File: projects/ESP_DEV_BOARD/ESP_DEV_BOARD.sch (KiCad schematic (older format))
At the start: 34 parts, among them CN1 MJ-179P, CN2 B6B-XH-A, CN3 DM3AT-SF-PEJM5, CN7 PH-1X10RG(2), SW1 SKHHBY, SW2 SKHHBY, SW3 SKHHBY, SW4 SKHHBY, U1 BME680, U2 CCS811

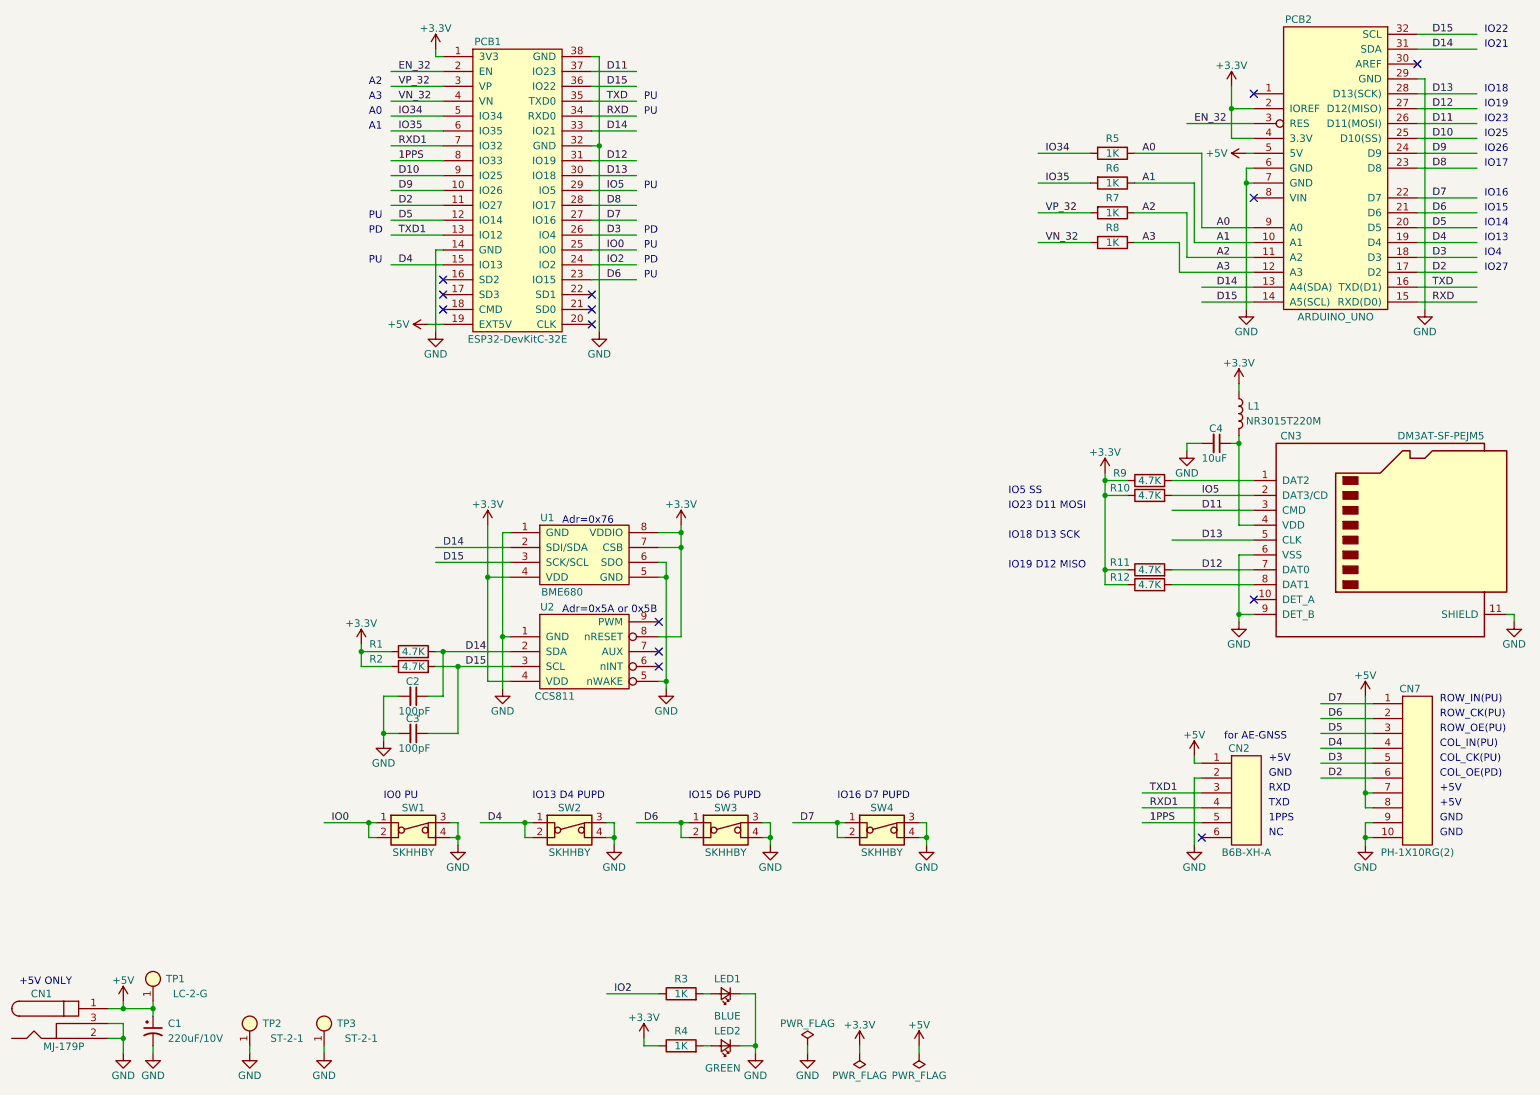
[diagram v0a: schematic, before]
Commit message: 赤外線送受信回路の追加。
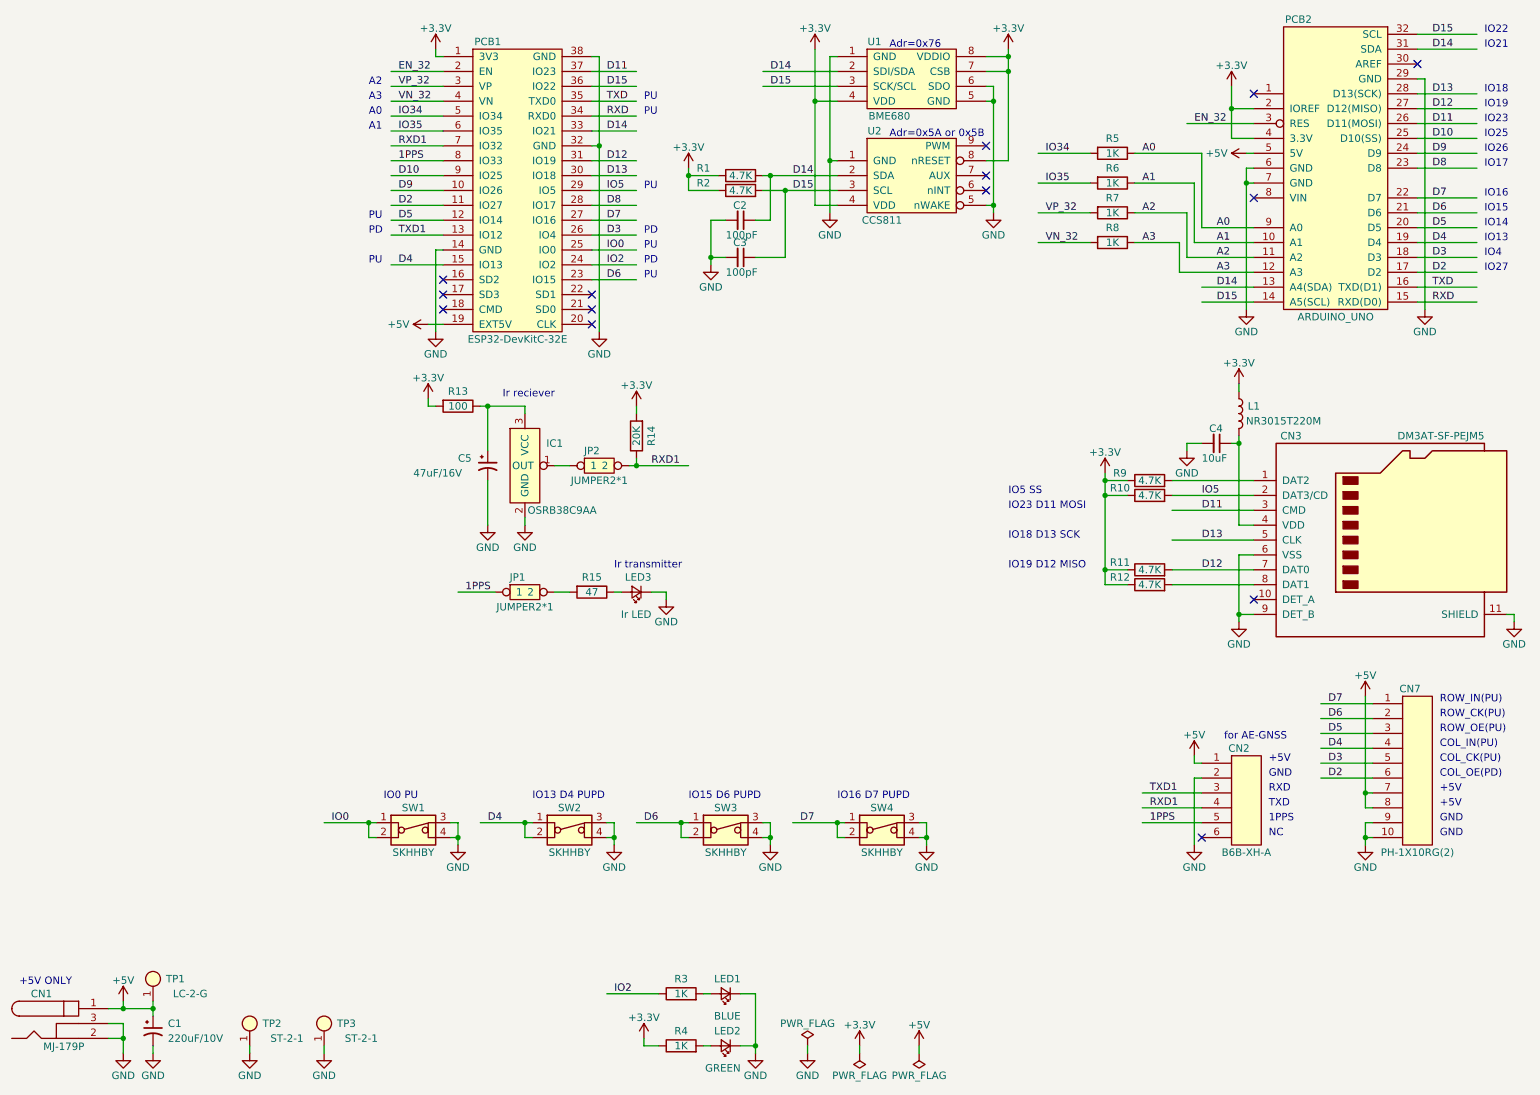
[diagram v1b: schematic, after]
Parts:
- added C5: 47uF/16V, A01myFootPrint:CP_Radial_D5.0mm_P2.00mm, symbol CP1_Small
- added IC1: OSRB38C9AA, A01myFootPrint:ic_OSRB38C9AA, symbol ic_OSRB38C9AA
- added JP1, JP2: JUMPER2*1, A01myFootPrint:JP_JUMPER1x2, symbol JUMPER2*1
- added LED3: Ir LED, A01myFootPrint:led_5mmLED, symbol LED
- added R13: 100, A01myFootPrint:C_0603, symbol R
- added R14: 20K, A01myFootPrint:C_0603, symbol R
- added R15: 47, A01myFootPrint:C_0603, symbol R
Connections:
- wire segments 192 -> 208
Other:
- note added: "Ir reciever"
- note added: "Ir transmitter"
- moved on the sheet: C2, C3, R1, R2, U1, U2

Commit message: .gitignoreファイルの更新と、部品表の追加。
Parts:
- C1, C5: symbol CP1_Small -> cp1_small:CP1_Small
- C2, C3, C4: symbol C_Small -> c_np_small:C_Small
- CN1: symbol BARREL_JACK -> cn_MJ-179P:BARREL_JACK
- CN2: symbol 6PIN -> cn_connectors:6PIN
- CN3: symbol Micro_SD_Card_Det_Hirose_DM3AT -> cn_micro_sd_card_det:Micro_SD_Card_Det_Hirose_DM3AT
- CN7: symbol 10PIN -> cn_connectors:10PIN
- IC1: symbol ic_OSRB38C9AA -> ic_osrb38c9aa:ic_OSRB38C9AA
- JP1, JP2: symbol JUMPER2*1 -> jp_JUMPER:JUMPER2*1
- L1: symbol L -> l_Inductor:L
- LED1, LED2, LED3: symbol LED -> led_LED3MM:LED
- PCB1: symbol pcb_ESP32-DevKitC-32E -> pcb_esp32-devkitc-32e:pcb_ESP32-DevKitC-32E
- PCB2: symbol pcb_ARDUINO_UNO -> pcb_arduino_uno:pcb_ARDUINO_UNO
- R1, R10, R11, R12, R13, R14, R15, R2, R3, R4, R5, R6, R7, R8, R9: symbol R -> r_register:R
- SW1, SW2, SW3, SW4: symbol SKHHBY -> sw_skhhby:SKHHBY
- TP1, TP2, TP3: symbol LC-2-G -> tb_lc-2-g:LC-2-G
- U1: symbol pcb_BME680_strawberry-linux -> pcb_bme680_strawberry-linux:pcb_BME680_strawberry-linux
- U2: symbol pcb_CCS811_strawberry-linux -> pcb_ccs811_strawberry-linux:pcb_CCS811_strawberry-linux
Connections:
- wire segments 208 -> 242
